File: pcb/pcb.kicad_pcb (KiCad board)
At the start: 2 copper layers, 149.6 x 66.4 mm, 34 parts, among them J1 Ribbon Cable Header, J2 Ribbon Cable Header, J3 UPDI, SW1 MX Grey w/ LED, SW2 MX Grey w/ LED, SW3 1241.1100.7095, SW4 SW_SPST, U1 Display Driver, U2 Display Driver, U3 MCU, U4 OR, 2 Channels, U5 Voltage Regulator, Y1 32.768 kHz

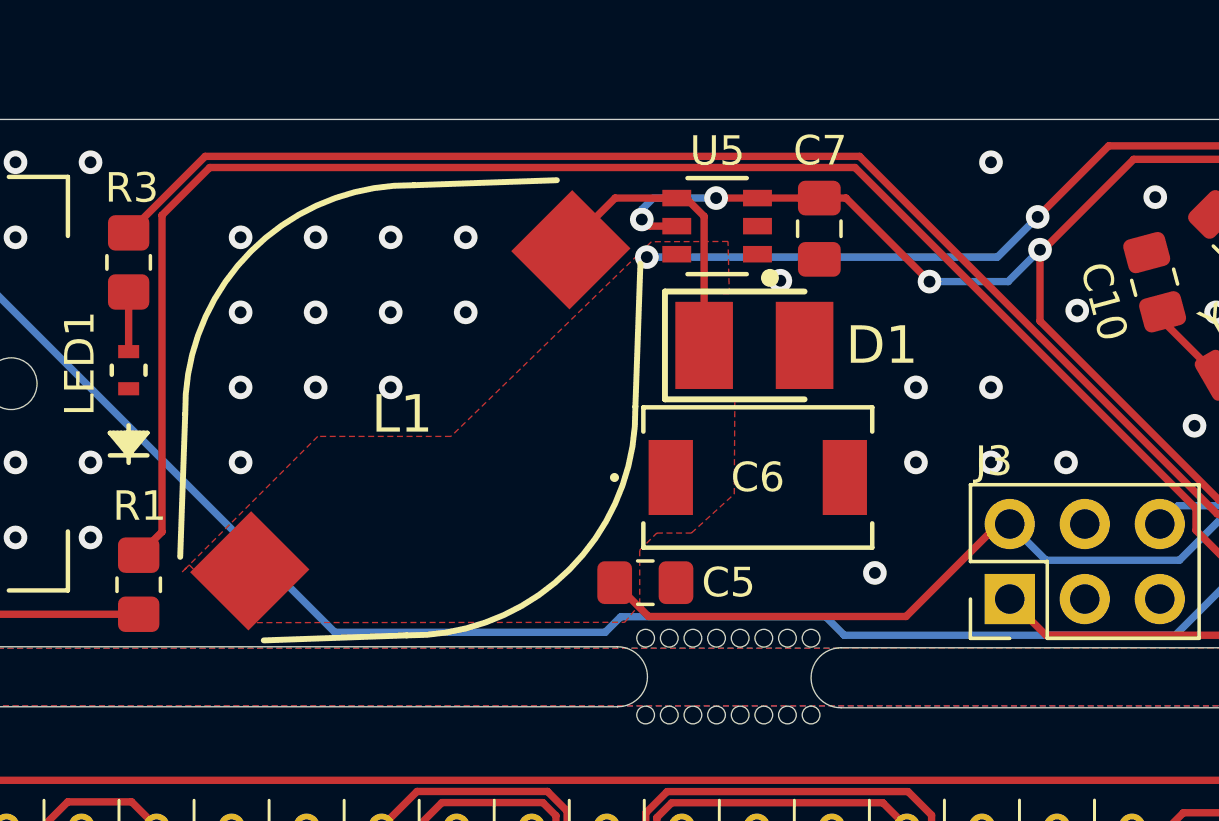
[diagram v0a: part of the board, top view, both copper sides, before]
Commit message: Move micro onto LCD board
Signed-off-by: Michael Darr <michael.e.darr@gmail.com>
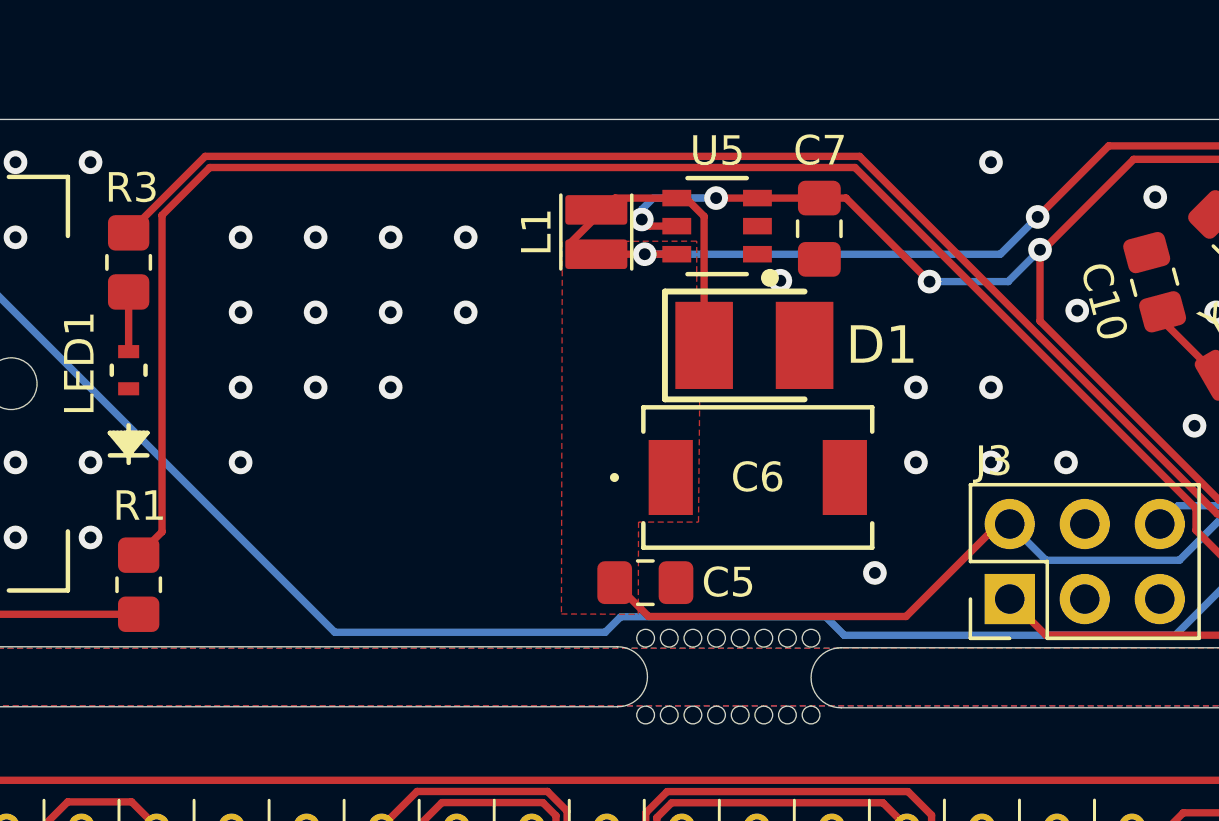
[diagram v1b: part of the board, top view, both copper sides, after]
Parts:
- L1: value 100μH -> 47μH; footprint chess_clock:DO5022P-104MLD -> chess_clock:Inductor_6060
- moved L1 8.72 mm to (107.8, 77.9), turned to 90 degrees
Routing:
- net VCC: track 116.4 -> 119.2 mm
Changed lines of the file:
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@@
     )
   )
-  (footprint "chess_clock:DO5022P-104MLD" (layer "F.Cu")
-    (at 101.504116 83.945884 45)
-    (descr "DO5022P-104MLD")
-    (tags "Inductor")
-    (property "PN" "DO5022P-104MLD")
+  (footprint "chess_clock:Inductor_6060" (layer "F.Cu")
+    (at 107.8 77.91177 90)
+    (descr "smd shielded power inductor 4x4x3mm, Abracon ASPI-4030S, https://abracon.com/Magnetics/power/ASPI-4030S.pdf")
+    (tags "inductor abracon smd shielded")
+    (property "PN" "HPC 6045NV-470M")
     (property "Sheetfile" "pcb.kicad_sch")
     (property "Sheetname" "")
@@
     (property "ki_keywords" "inductor choke coil reactor magnetic")
     (attr smd)
-    (fp_text reference "L1" (at -0.291001 -0.099) (layer "F.SilkS")
-        (effects (font (size 1.27 1.27) (thickness 0.254)))
+    (fp_text reference "L1" (at 0 -2.01 90) (layer "F.SilkS")
+        (effects (font (size 1 1) (thickness 0.15)))
     )
-    (fp_text value "100μH" (at 1.615114 -2.180799) (layer "F.SilkS") hide
-        (effects (font (size 1.27 1.27) (thickness 0.254)))
+    (fp_text value "47μH" (at -0.01 1.93 90) (layer "F.Fab")
+        (effects (font (size 1 1) (thickness 0.15)))
     )
-    (fp_text user "${REFERENCE}" (at -0.291001 -0.099) (layer "F.Fab")
-        (effects (font (size 1.27 1.27) (thickness 0.254)))
+    (fp_text user "${REFERENCE}" (at 0 3.26 90) (layer "F.Fab")
+        (effects (font (size 1 1) (thickness 0.15)))
     )
-    (fp_line (start -9.015 2) (end -5.47489 5.3)
-      (stroke (width 0.2) (type solid)) (layer "F.SilkS"))
-    (fp_line (start -5.47489 -5.3) (end -9.015 -2)
-      (stroke (width 0.2) (type solid)) (layer "F.SilkS"))
-    (fp_line (start 5.47489 -5.3) (end 9.015 -2)
-      (stroke (width 0.2) (type solid)) (layer "F.SilkS"))
-    (fp_line (start 5.47489 5.3) (end 9.015 2)
-      (stroke (width 0.2) (type solid)) (layer "F.SilkS"))
-    (fp_arc (start -5.478607 -5.296158) (mid -0.002673 -7.620001) (end 5.47489 -5.3)
-      (stroke (width 0.2) (type solid)) (layer "F.SilkS"))
-    (fp_arc (start 5.478607 5.296158) (mid 0.002673 7.620001) (end -5.47489 5.3)
-      (stroke (width 0.2) (type solid)) (layer "F.SilkS"))
-    (fp_line (start -9.015 -2) (end -9.015 2)
-      (stroke (width 0.05) (type default)) (layer "F.CrtYd"))
-    (fp_line (start -9.015 2) (end -5.47489 5.3)
-      (stroke (width 0.1) (type solid)) (layer "F.CrtYd"))
-    (fp_line (start -5.47489 -5.3) (end -9.015 -2)
-      (stroke (width 0.1) (type solid)) (layer "F.CrtYd"))
-    (fp_line (start 5.47489 -5.3) (end 9.015 -2)
-      (stroke (width 0.1) (type solid)) (layer "F.CrtYd"))
-    (fp_line (start 5.47489 5.3) (end 9.015 2)
-      (stroke (width 0.1) (type solid)) (layer "F.CrtYd"))
-    (fp_line (start 9.015 -2) (end 9.015 2)
-      (stroke (width 0.05) (type default)) (layer "F.CrtYd"))
-    (fp_arc (start -5.478607 -5.296158) (mid -0.002673 -7.620001) (end 5.47489 -5.3)
-      (stroke (width 0.1) (type solid)) (layer "F.CrtYd"))
-    (fp_arc (start 5.478607 5.296158) (mid 0.002673 7.620001) (end -5.47489 5.3)
-      (stroke (width 0.1) (type solid)) (layer "F.CrtYd"))
-    (fp_line (start -9.015 -2) (end -9.015 2)
-      (stroke (width 0.2) (type solid)) (layer "F.Fab"))
-    (fp_line (start 9.015 -2) (end 9.015 2)
-      (stroke (width 0.2) (type solid)) (layer "F.Fab"))
-    (pad "1" smd rect (at -7.685 0 135) (size 2.79 2.92) (layers "F.Cu" "F.Paste" "F.Mask")
+    (fp_line (start -1.25 -1.2) (end 1.25 -1.2)
+      (stroke (width 0.12) (type solid)) (layer "F.SilkS"))
+    (fp_line (start -1.25 1.2) (end 1.25 1.2)
+      (stroke (width 0.12) (type solid)) (layer "F.SilkS"))
+    (fp_rect (start -1.28 -1.08) (end 1.28 1.08)
+      (stroke (width 0.05) (type default)) (fill none) (layer "F.CrtYd"))
+    (pad "1" smd roundrect (at -0.75 0 90) (size 1 2.1) (layers "F.Cu" "F.Paste" "F.Mask") (roundrect_rratio 0.1)
       (net 99 "VCC") (pinfunction "1") (pintype "passive"))
-    (pad "2" smd rect (at 7.685 0 135) (size 2.79 2.92) (layers "F.Cu" "F.Paste" "F.Mask")
+    (pad "2" smd roundrect (at 0.75 0 90) (size 1 2.1) (layers "F.Cu" "F.Paste" "F.Mask") (roundrect_rratio 0.1)
       (net 87 "Net-(D1-K)") (pinfunction "2") (pintype "passive"))
-    (model "${KIPRJMOD}/Clock-Parts.3dshapes/DO5022P-104MLD.step"
+    (model "${KICAD6_3DMODEL_DIR}/Inductor_SMD.3dshapes/L_Abracon_ASPI-4030S.wrl"
       (offset (xyz 0 0 0))
       (scale (xyz 1 1 1))
-      (rotate (xyz -90 0 90))
+      (rotate (xyz 0 0 0))
     )
   )
@@
   (segment (start 136.905643 85.608256) (end 136.905643 85.3725) (width 0.25) (layer "F.Cu") (net 99))
   (segment (start 161.628632 82.526) (end 176.369158 82.526) (width 0.25) (layer "F.Cu") (net 99))
+  (segment (start 107.8 78.66177) (end 110.52475 78.66177) (width 0.25) (layer "F.Cu") (net 99))
   (segment (start 178.45 87.58) (end 178.28 87.75) (width 0.25) (layer "F.Cu") (net 99))
   (segment (start 118.284706 90.925294) (end 121.415 87.795) (width 0.25) (layer "F.Cu") (net 99))
@@
   (segment (start 109.567794 90.925294) (end 118.284706 90.925294) (width 0.25) (layer "F.Cu") (net 99))
   (segment (start 178.45 84.606842) (end 178.45 87.58) (width 0.25) (layer "F.Cu") (net 99))
-  (via (at 109.51 78.76) (size 0.8) (drill 0.4) (layers "F.Cu" "B.Cu") (net 99))
+  (via (at 109.44 78.66177) (size 0.8) (drill 0.4) (layers "F.Cu" "B.Cu") (net 99))
   (via (at 136.905643 85.3725) (size 0.8) (drill 0.4) (layers "F.Cu" "B.Cu") (net 99))
   (via (at 139.07 87.4475) (size 0.8) (drill 0.4) (layers "F.Cu" "B.Cu") (net 99))
@@
   (segment (start 129.008128 87.551872) (end 129.692822 87.551872) (width 0.25) (layer "B.Cu") (net 99))
   (segment (start 121.795 87.795) (end 123.02 89.02) (width 0.25) (layer "B.Cu") (net 99))
-  (segment (start 121.38 78.76) (end 122.74 77.4) (width 0.25) (layer "B.Cu") (net 99))
-  (segment (start 109.51 78.76) (end 121.38 78.76) (width 0.25) (layer "B.Cu") (net 99))
+  (segment (start 109.44 78.66177) (end 121.47823 78.66177) (width 0.25) (layer "B.Cu") (net 99))
+  (segment (start 121.47823 78.66177) (end 122.74 77.4) (width 0.25) (layer "B.Cu") (net 99))
   (segment (start 133.968143 88.31) (end 136.905643 85.3725) (width 0.25) (layer "B.Cu") (net 99))
   (segment (start 136.995 85.3725) (end 139.07 87.4475) (width 0.25) (layer "B.Cu") (net 99))
@@
     (polygon
       (pts
-        (xy 95.983831 91.133902)
-        (xy 108.762039 91.122556)
-        (xy 109.27 90.51375)
-        (xy 109.27 88.68)
-        (xy 109.85 88.1)
-        (xy 111.02 88.1)
-        (xy 112.47 86.78)
-        (xy 112.49 83.53)
+        (xy 109.22 90.85)
+        (xy 109.23 87.73)
+        (xy 111.26 87.73)
+        (xy 111.3 83.52)
         (xy 110.14 83.52)
         (xy 110.13 79.92)
-        (xy 112.302212 80.003485)
-        (xy 112.259371 78.230197)
-        (xy 109.665212 78.240213)
-        (xy 102.88 84.83)
-        (xy 98.37 84.83)
-        (xy 93.78 89.42)
-        (xy 94.021101 89.178899)
+        (xy 111.2 79.92)
+        (xy 111.199371 78.220197)
+        (xy 106.65 78.23)
+        (xy 106.62 90.84)
       )
     )

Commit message: Redo pcb layout
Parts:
- removed SW4: SW_SPST, chess_clock:CWSA11AAN1H
- added R5: 2.7kΩ, Resistor_SMD:R_0805_2012Metric_Pad1.20x1.40mm_HandSolder, F.Cu at (161.2, 109.5)
- added R6: 27kΩ, Resistor_SMD:R_0805_2012Metric_Pad1.20x1.40mm_HandSolder, F.Cu at (209.5, 79.4)
- added R7: 12kΩ, Resistor_SMD:R_0805_2012Metric_Pad1.20x1.40mm_HandSolder, F.Cu at (160.2, 89.1)
- J1, J2: value Ribbon Cable Header -> Conn_01x04; footprint chess_clock:903250014 -> chess_clock:2005290040
- LCD1, LCD2, SW1, SW2, SW3: moved to B.Cu
- R4: value 50Ω -> 2.7kΩ; footprint chess_clock:352151RFT -> Resistor_SMD:R_0805_2012Metric_Pad1.20x1.40mm_HandSolder
- Y1: value 32.768 kHz -> 32kHz
- moved C1 140.3 mm to (215.8, 105.1), turned to -90 degrees
- moved U1 139.4 mm to (215.8, 108.5), turned to -90 degrees
- moved SW2 139.2 mm to (76.8, 84.5), turned to 180 degrees
- moved SW1 139.1 mm to (222.0, 84.5), turned to 180 degrees
- moved R2 117.5 mm to (89.1, 89.6), turned to 0 degrees
- moved R1 117.2 mm to (209.5, 89.6), turned to 180 degrees
- moved LCD2 90.1 mm to (107.4, 115.5)
- moved LCD1 89.7 mm to (191.4, 115.5)
- moved R3 75.6 mm to (142.2, 135.5), turned to 0 degrees
- moved LED1 70.4 mm to (138.5, 135.5), turned to 0 degrees
- moved J3 53.0 mm to (150.7, 134.7), turned to 180 degrees
- moved C10 51.5 mm to (135.3, 130.4), turned to 15 degrees
- moved C9 49.8 mm to (133.7, 127.7), turned to 45 degrees
- moved C2 48.3 mm to (131.3, 105.1), turned to -90 degrees
- moved R4 47.5 mm to (89.1, 79.4)
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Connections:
- net /LED1_ENABLE renamed /BAT_LOW_LED
- net UDPI renamed UPDI
- BT1 pad 1: Net-(BT1-+) -> VBAT
- BT1 pad 2: Net-(BT1--) -> GND
- C1 pad 1: VSS -> GND
- C1 pad 2: VDD -> VCC
- C2 pad 1: VSS -> GND
- C2 pad 2: VDD -> VCC
- C4 pad 1: VDD -> VCC
- C4 pad 2: VSS -> GND
- C7 pad 1: VBAT_PROT -> VBAT
- J1 pad 1: LCD_COL_2 -> /SW2_LED
- J1 pad 2: GND -> VCC
- J1 pad 3: LCD_LATCH_2 -> /SW1_LED
- J1 pad 4: LCD_COL_1 -> GND
- J1 pad 5: LCD_DATA0 -> GND
- J1 pad 6: LCD_DATA1 -> GND
- J2 pad 1: /BUZZ -> Net-(J2-Pad1)
- J2 pad 2: VDD -> Net-(J2-Pad2)
- J2 pad 3: WRITE -> Net-(J2-Pad3)
- J2 pad 4: LATCH_1 -> GND1
- J2 pad 5: DIGIT2 -> GND1
- J2 pad 6: DIGIT1 -> GND1
- LS1 pad 1: /BUZZ -> VCC
- LS1 pad 2: VSS -> /BUZZ
- R1 pad 1: /SW1_LED_ENABLE -> Net-(SW1-A)
- R1 pad 2: Net-(SW1-A) -> Net-(J2-Pad3)
- R2 pad 1: /SW2_LED_ENABLE -> Net-(SW2-A)
- R2 pad 2: Net-(SW2-A) -> Net-(J2-Pad1)
- R4 pad 1: Net-(BT1-+) -> Net-(J2-Pad2)
- R4 pad 2: VBAT_PROT -> Net-(R4-Pad2)
- SW1 pad 1: GND -> GND1
- SW1 pad 2: /~{SW1_ACTIVE} -> Net-(R6-Pad1)
- SW1 pad 3: GND -> GND1
- SW2 pad 1: GND -> GND1
- SW2 pad 2: /~{SW2_ACTIVE} -> Net-(R4-Pad2)
- SW2 pad 3: GND -> GND1
- SW3 pad 1: GND -> Net-(R7-Pad1)
- SW3 pad 2: /~{SW3_ACTIVE} -> GND1
- U1 pad 1: VDD -> VCC
- U1 pad 34: WRITE -> LCD_WRITE
- U1 pad 35: VSS -> GND
- U2 pad 1: VDD -> VCC
- U2 pad 34: WRITE -> LCD_WRITE
- U2 pad 35: VSS -> GND
- U2 pad 36: VSS -> GND
- U3 pad 1: LCD_LATCH_1 -> LATCH_1
- U3 pad 10: LCD_DIGIT1 -> DIGIT1
- U3 pad 11: LCD_COL_2 -> COL_2
- U3 pad 12: LCD_COL_1 -> COL_1
- U3 pad 15: VBAT_PROT -> VBAT
- U3 pad 17: /~{SW1_ACTIVE} -> /SW1_LED
- U3 pad 18: /SW1_LED_ENABLE -> /SW_READ
- U3 pad 19: /~{SW2_ACTIVE} -> /SW2_LED
- U3 pad 2: LCD_LATCH_2 -> LATCH_2
- U3 pad 20: /SW2_LED_ENABLE -> unconnected-(U3-PC3-Pad20)
- U3 pad 21: /~{SW3_ACTIVE} -> /BUZZ
- U3 pad 22: LCD_BUZZ -> unconnected-(U3-PC5-Pad22)
- U3 pad 5: LCD_DATA0 -> DATA0
- U3 pad 6: LCD_DATA1 -> DATA1
- U3 pad 7: LCD_DATA2 -> DATA2
- U3 pad 8: LCD_DATA3 -> DATA3
- U3 pad 9: LCD_DIGIT2 -> DIGIT2
- U4 pad 4: VSS -> GND
- U4 pad 8: VDD -> VCC
- U5 pad 3: VBAT_PROT -> VBAT
- U5 pad 5: VBAT_PROT -> VBAT
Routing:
- net BP: track 417.5 -> 0.00 mm, vias 1 -> 0
- net VDD: track 171.1 -> 0.00 mm, vias 1 -> 0
- net Net-(J2-Pad2): track 0.00 -> 130.0 mm
- net DIGIT1: track 113.6 -> 0.00 mm
- net DATA0: track 112.4 -> 0.00 mm
- net DATA2: track 111.4 -> 0.00 mm
- net DATA1: track 106.9 -> 0.00 mm
- net DATA3: track 105.6 -> 0.00 mm
- net DIGIT2: track 105.4 -> 0.00 mm
- net WRITE: track 105.4 -> 0.00 mm
- net /LCD2.A2: track 99.4 -> 0.00 mm
- net /~{SW2_ACTIVE}: track 96.9 -> 0.00 mm, vias 1 -> 0
- net /LCD2.B2: track 95.6 -> 0.00 mm
- net /LCD2.G2: track 92.7 -> 0.00 mm
- net /LCD1.G2: track 91.4 -> 0.00 mm
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- added copper zone on B.Cu, net GND1
- added copper zone on F.Cu, net GND1
- removed copper zone on B.Cu, net VSS
- removed copper zone on F.Cu, net VSS
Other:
- board size 149.6 x 66.4 mm -> 159.6 x 59.6 mm
- board text added: "0.3.0"
- board text removed: "0.2.0"

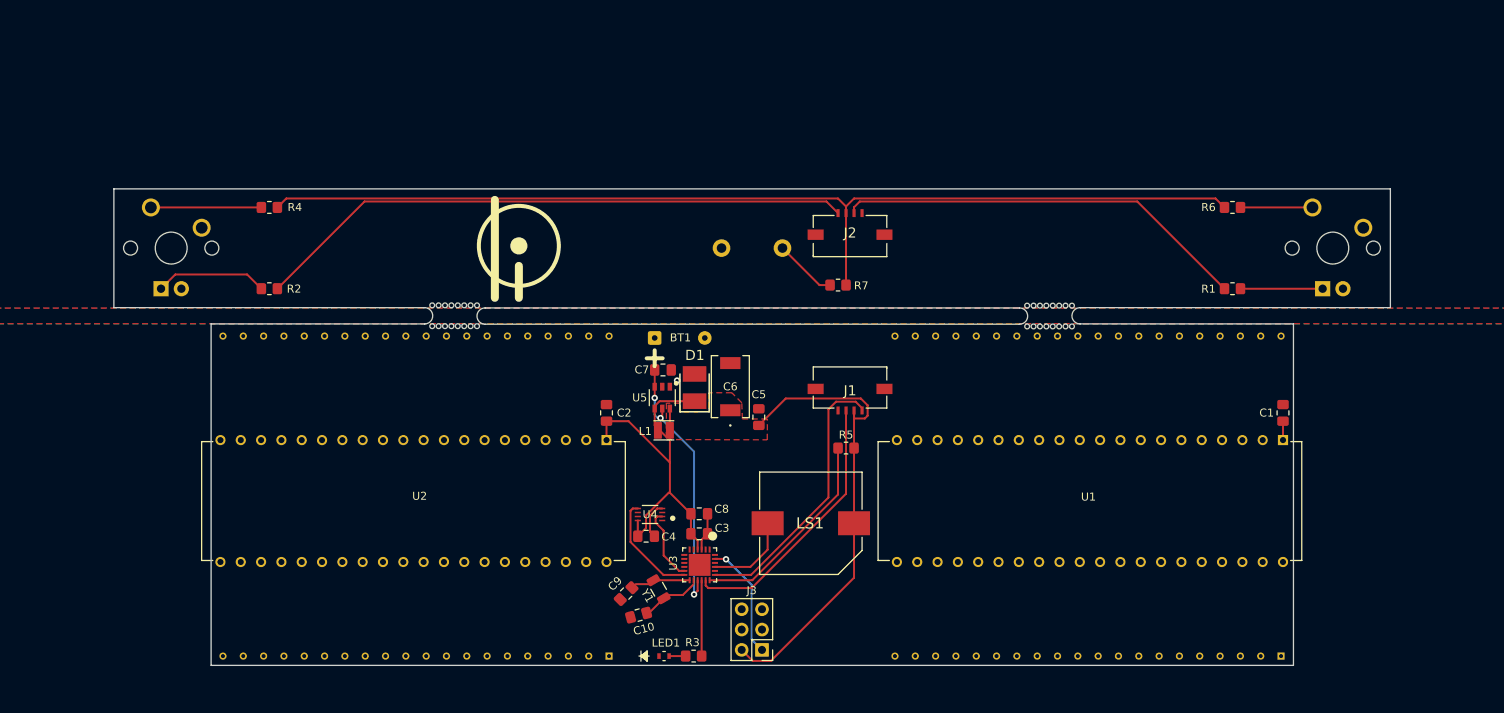
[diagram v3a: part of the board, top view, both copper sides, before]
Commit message: Finalize initial design
Signed-off-by: Michael Darr <mdarr@tesla.com>
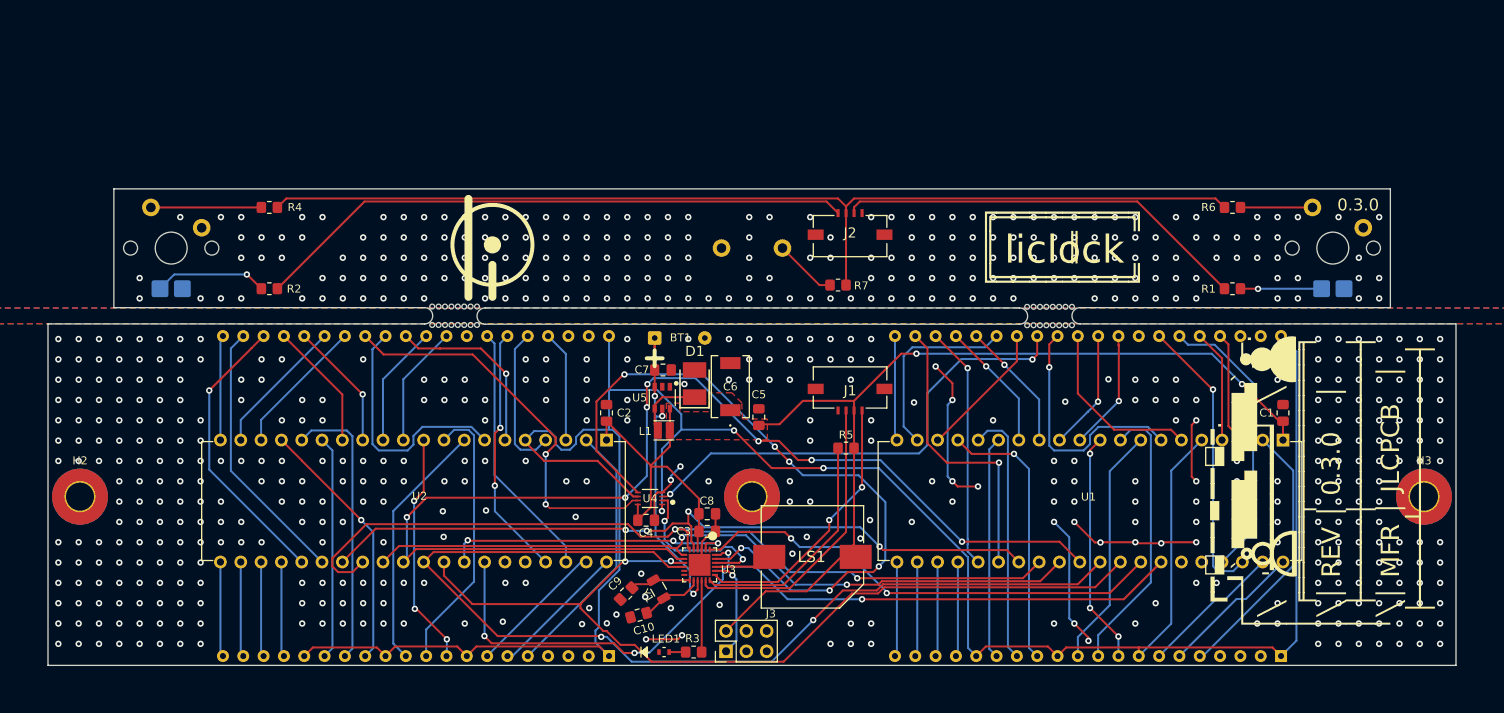
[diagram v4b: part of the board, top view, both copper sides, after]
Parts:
- added H1: MountingHole_Pad, MountingHole:MountingHole_3.5mm_Pad_TopBottom, F.Cu at (149.4, 115.6)
- added H2: MountingHole_Pad, MountingHole:MountingHole_3.5mm_Pad_TopBottom, F.Cu at (65.4, 115.6)
- added H3: MountingHole_Pad, MountingHole:MountingHole_3.5mm_Pad_TopBottom, F.Cu at (233.4, 115.6)
- moved J3 4.50 mm to (146.2, 134.9), turned to 90 degrees
- moved LS1 4.20 mm to (157.0, 123.1)
- moved U4 2.00 mm to (136.7, 115.8)
- moved C4 2.00 mm to (136.2, 118.5)
- moved C3 1.04 mm to (143.8, 119.9)
- moved C8 1.00 mm to (143.8, 117.7)
- moved D1 0.50 mm to (142.3, 101.4)
- moved LED1 0.50 mm to (138.5, 135.0)
- moved R3 0.50 mm to (142.2, 135.0)
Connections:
- U3 pad 11: COL_2 -> unconnected-(U3-PB5-Pad11)
- U3 pad 12: COL_1 -> unconnected-(U3-PB4-Pad12)
- U3 pad 20: unconnected-(U3-PC3-Pad20) -> UPDI
- U3 pad 22: unconnected-(U3-PC5-Pad22) -> COL_2
- U3 pad 23: UPDI -> COL_1
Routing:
- net BP: track 0.00 -> 307.0 mm, vias 0 -> 3
- net DATA3: track 0.00 -> 149.6 mm, vias 0 -> 7
- net DIGIT1: track 0.00 -> 128.7 mm, vias 0 -> 2
- net DIGIT2: track 0.00 -> 111.5 mm, vias 0 -> 2
- net LCD_WRITE: track 0.00 -> 107.0 mm, vias 0 -> 4
- net DATA1: track 0.00 -> 104.1 mm, vias 0 -> 2
- net DATA0: track 0.00 -> 94.4 mm, vias 0 -> 4
- net DATA2: track 0.00 -> 91.7 mm, vias 0 -> 2
- net COL_1: track 13.4 -> 90.6 mm, vias 0 -> 6
- net GND: track 9.47 -> 80.7 mm, vias 1 -> 430
- net COL_BP_1: track 0.00 -> 60.5 mm, vias 0 -> 2
- net LATCH_1: track 0.00 -> 59.6 mm, vias 0 -> 2
- net VCC: track 102.4 -> 158.2 mm, vias 0 -> 2
- net COL_BP_2: track 0.00 -> 50.0 mm, vias 0 -> 2
- net LATCH_2: track 0.00 -> 36.8 mm, vias 0 -> 3
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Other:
- board size 159.6 x 59.6 mm -> 176 x 59.6 mm
- board text added: "┏━⬓━━▬━━⬓━. ┌──┚`▝███▖▜██▙`ˎ─. │╲ ꞌ━━━━━━━━━┙ ╲ │ ╒═════╤══════════╕ │╲│ REV │ 0.3.0 │ │ ├─────┼──────────┤ ╵╲│ MFR │ JLCPCB │ ├─────┴──────────┤"
- board text removed: "┏━⬓━━▬━━⬓━. ┌──┚`▝███▖▜██▙`ˎ─. │╲ ꞌ━━━━━━━━━┙ ╲ │ ╒═════╤══════════╕ │╲│ REV │ 0.2.0 │ │ ├─────┼──────────┤ ╵╲│ MFR │ JLCPCB │ ├─────┴──────────┤"
